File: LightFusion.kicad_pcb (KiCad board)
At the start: 2 copper layers, 52 x 52 mm, 30 parts, among them J1 303C-C4115-30-04, P1 PHR-2, U1 BMD-350-A-R, U2 TPS7A2033PDBVR, U3 TPS22918DBVR

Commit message: placement finished on PCB
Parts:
- added C_ADC_AVDD_BULK1: 100 nF, LightFusion:C_0603_1608Metric, F.Cu at (149.9, 142.6)
- added C_ADC_AVDD_BYP1: 100 nF, LightFusion:C_0603_1608Metric, F.Cu at (151.5, 142.6)
- added C_ADC_DVDD_BULK1: 1uF, LightFusion:C_0603_1608Metric, F.Cu at (156.6, 143.5)
- added C_ADC_DVDD_BYP1: 100 nF, LightFusion:C_0603_1608Metric, F.Cu at (158.8, 145.2)
- added C_ADC_PHOTO_N1: 100nF, LightFusion:C_0603_1608Metric, F.Cu at (147.3, 150.9)
- added C_ADC_PHOTO_P1: 100nF, LightFusion:C_0603_1608Metric, F.Cu at (147.3, 149.4)
- added C_ADC_REF_BULK1: 10uF, LightFusion:C_0603_1608Metric, F.Cu at (147.2, 144.5)
- added C_ADC_REF_BYP1: 100 nF, LightFusion:C_0603_1608Metric, F.Cu at (147.2, 146.2)
- added C_PD_BIAS1: 10uF, LightFusion:C_0603_1608Metric, F.Cu at (145.0, 135.6)
- added C_PD_FB1: 6.8pF, LightFusion:C_0603_1608Metric, F.Cu at (141.3, 140.5)
- added C_PD_TIA_SUPPLY1: 1 µF, LightFusion:C_0603_1608Metric, F.Cu at (143.0, 144.7)
- added D_PD1: VEMD8082, LightFusion:VEMD8082, F.Cu at (150.1, 137.3)
- added IC1: MCP3561T-E_ST, LightFusion:MCP3561T-E_ST, F.Cu at (153.1, 148.1)
- added R_ADC_CS_PU1: 10k, LightFusion:R_0603_1608Metric, F.Cu at (158.8, 147.1)
- added R_ADC_IRQ_PU1: 10k, LightFusion:R_0603_1608Metric, F.Cu at (158.8, 149.6)
- added R_ADC_PHOTO_N1: 100R, LightFusion:R_0603_1608Metric, F.Cu at (147.3, 152.5)
- added R_ADC_PHOTO_P1: 100R, LightFusion:R_0603_1608Metric, F.Cu at (147.3, 147.8)
- added R_PD_BIAS_BOT1: 1.8k, LightFusion:R_0603_1608Metric, F.Cu at (143.4, 135.6)
- added R_PD_BIAS_TOP1: 10k, LightFusion:R_0603_1608Metric, F.Cu at (141.8, 135.6)
- added R_PD_FB1: 10k, LightFusion:R_0603_1608Metric, F.Cu at (139.8, 140.5)
- added R_PD_SUPPLY1: 10R, LightFusion:R_0603_1608Metric, F.Cu at (140.2, 135.7)
- added U_PD_TIA1: OPA381AIDGKR, LightFusion:OPA381AIDGKR, F.Cu at (143.9, 140.6)
- C730_BYP1, C850_BYP1, CSLOPE_730, CSLOPE_850, C_M1, C_M2, C_PWR3, C_PWR4, C_PWR_SW_CT1, C_TEMP1: footprint LightFusion:C_0402_1005Metric -> LightFusion:C_0603_1608Metric
- J1: footprint LightFusion:303D-L186M020 -> LightFusion:303D-L186F020
- R1, R2, R_ON_PD1, R_TEMP_ALERT1: footprint LightFusion:R_0402_1005Metric -> LightFusion:R_0603_1608Metric
- moved U1 15.6 mm to (164.0, 115.1), turned to -135 degrees
- moved R2 12.8 mm to (158.5, 118.4), turned to 45 degrees
- moved C_M2 12.3 mm to (161.2, 120.9), turned to -135 degrees
- moved R1 11.9 mm to (159.8, 119.6), turned to 45 degrees
- moved J_PROG1 7.86 mm to (167.8, 124.1), turned to 180 degrees
- moved C_PWR3 7.84 mm to (147.6, 120.0)
- moved C_M1 7.22 mm to (165.6, 120.5), turned to 0 degrees
- moved U2 7.18 mm to (149.7, 122.8)
- moved C_PWR4 7.16 mm to (150.9, 120.0)
- moved C_PWR_SW_CT1 6.20 mm to (153.4, 123.3), turned to 90 degrees
- moved U3 5.66 mm to (154.6, 119.4)
- moved R_ON_PD1 3.45 mm to (155.7, 113.6)
- moved CSLOPE_850 1.38 mm to (167.6, 129.0), turned to 0 degrees
- moved U_TEMP1 1.22 mm to (150.0, 128.8)
- moved R_TEMP_ALERT1 0.72 mm to (149.1, 131.5)
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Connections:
- U1 pad 10: unconnected-(U1-P0.17-Pad10) -> ADC_MISO
- U1 pad 11: unconnected-(U1-P0.15-Pad11) -> ADC_SCK
- U1 pad 13: unconnected-(U1-P0.12-Pad13) -> ADC_CS_N
- U1 pad 42: unconnected-(U1-P0.19-Pad42) -> ADC_DRDY_N
- U1 pad 8: unconnected-(U1-P0.18-Pad8) -> ADC_MOSI

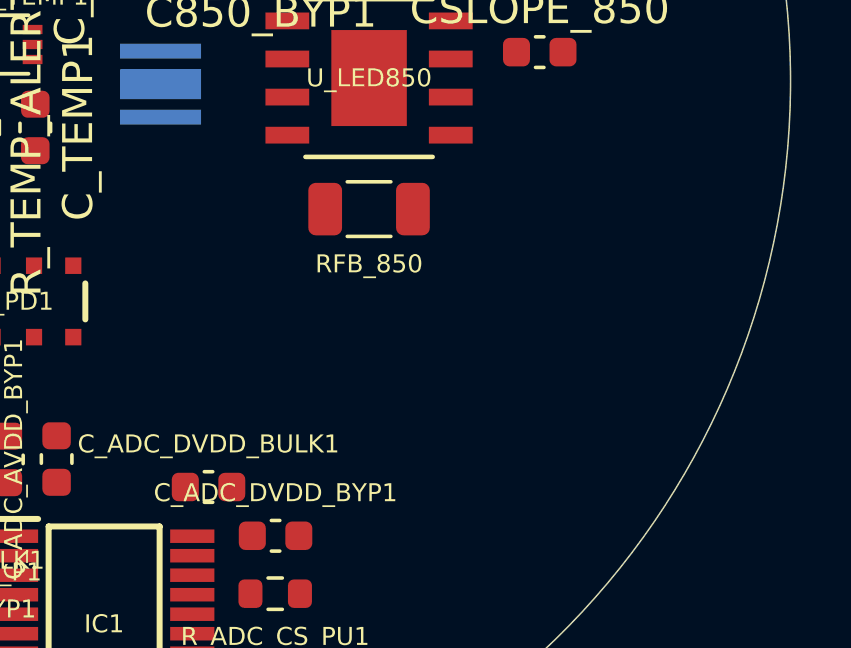
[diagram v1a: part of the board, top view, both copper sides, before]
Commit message: eeg ic was added
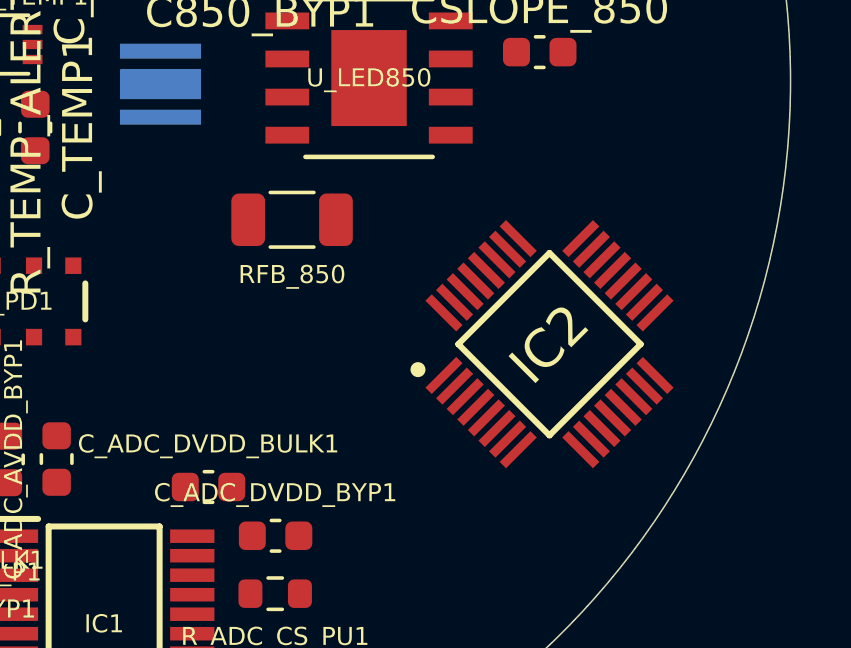
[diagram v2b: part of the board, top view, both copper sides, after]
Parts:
- added IC2: ADS1291IPBSR, LightFusion:ADS1291IPBSR, F.Cu at (168.0, 138.8)
- moved RFB_850 2.59 mm to (159.4, 134.6)

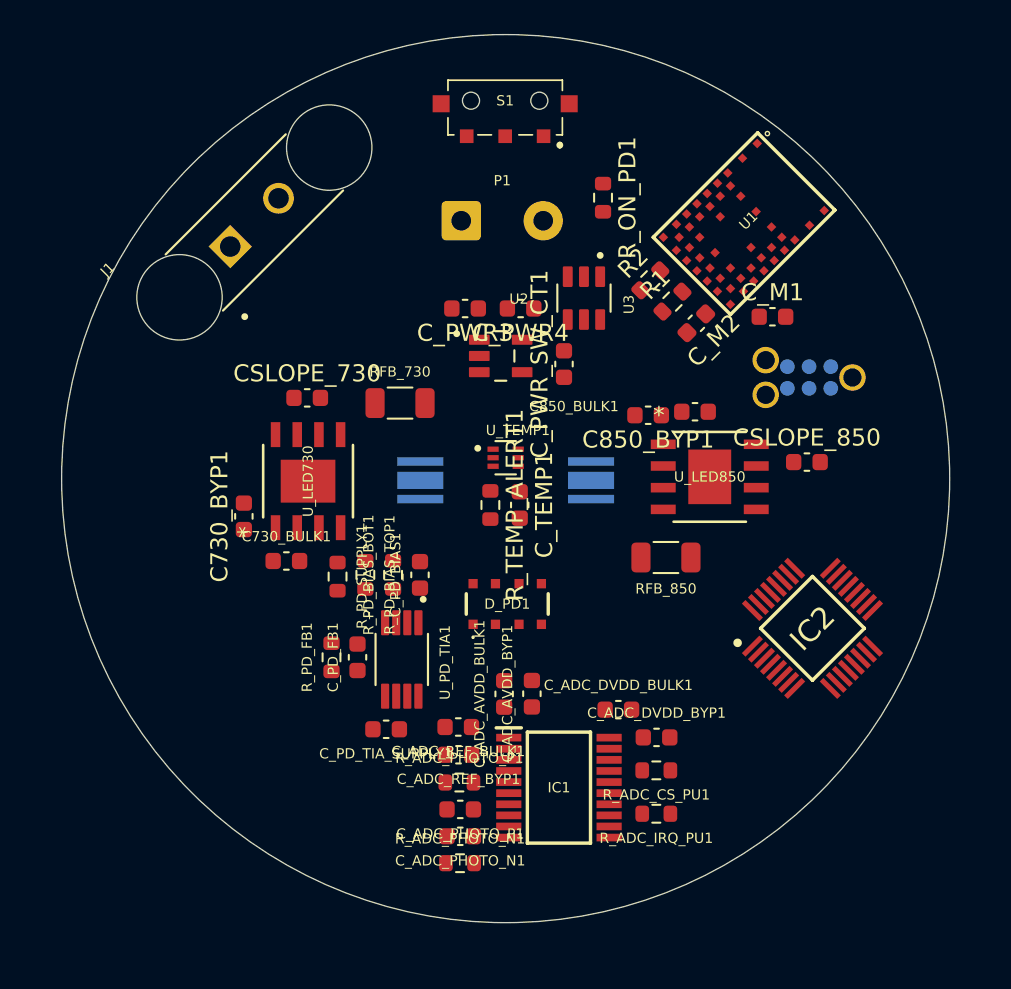
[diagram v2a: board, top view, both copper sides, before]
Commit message: eeg part refactored electrodes
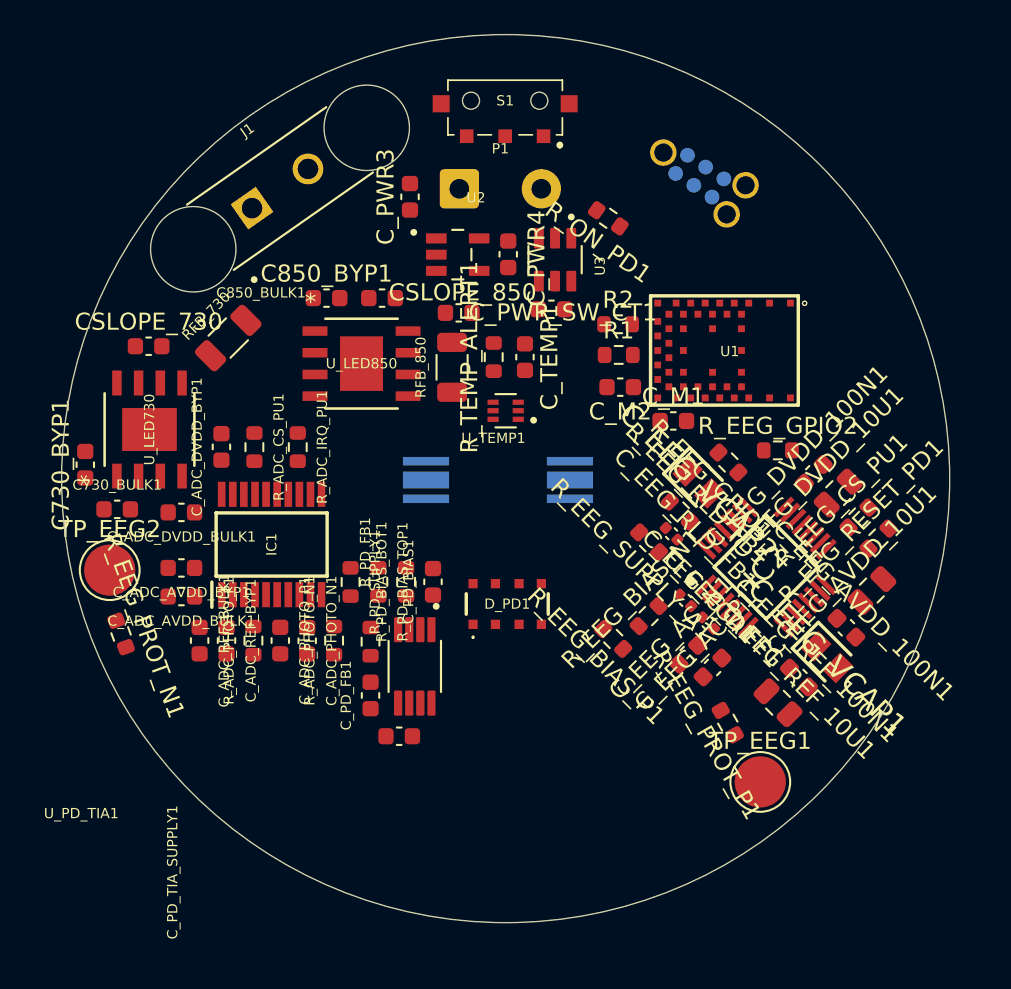
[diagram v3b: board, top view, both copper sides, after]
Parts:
- added C_EEG_AC_N1: 47 nF, LightFusion:C_0603_1608Metric, F.Cu at (160.7, 140.3)
- added C_EEG_AC_P1: 47 nF, LightFusion:C_0603_1608Metric, F.Cu at (162.1, 141.1)
- added C_EEG_AVDD_100N1: 100 nF, LightFusion:C_0603_1608Metric, F.Cu at (169.9, 138.7)
- added C_EEG_AVDD_10U1: 10 µF, LightFusion:C_0805_2012Metric, F.Cu at (171.4, 136.6)
- added C_EEG_DIFF1: 2.2 nF, LightFusion:C_0402_1005Metric, F.Cu at (161.9, 138.5)
- added C_EEG_DVDD_100N1: 100 nF, LightFusion:C_0603_1608Metric, F.Cu at (168.0, 129.7)
- added C_EEG_DVDD_10U1: 10 µF, LightFusion:C_0805_2012Metric, F.Cu at (169.5, 130.8)
- added C_EEG_PGA1: 4.7 nF, LightFusion:C_0402_1005Metric, F.Cu at (160.5, 137.1)
- added C_EEG_REF_100N1: 100 nF, LightFusion:C_0603_1608Metric, F.Cu at (167.2, 141.7)
- added C_EEG_REF_10U1: 10 µF, LightFusion:C_0805_2012Metric, F.Cu at (165.9, 143.1)
- added C_EEG_RLD_FB1: 1.5 nF, LightFusion:C_0402_1005Metric, F.Cu at (159.7, 133.2)
- added C_EEG_VCAP1: 1 µF, LightFusion:CAPPC2012X90N, F.Cu at (168.8, 140.5)
- added C_EEG_VCAP2: 1 µF, LightFusion:CAPPC2012X90N, F.Cu at (161.3, 130.2)
- added R_EEG_BIAS_N1: 22 MΩ, LightFusion:R_0603_1608Metric, F.Cu at (158.4, 138.0)
- added R_EEG_BIAS_P1: 22 MΩ, LightFusion:R_0603_1608Metric, F.Cu at (156.3, 139.4)
- added R_EEG_CS_PU1: 100 kΩ, LightFusion:R_0603_1608Metric, F.Cu at (170.7, 132.3)
- added R_EEG_GPIO1: 10 kΩ, LightFusion:R_0603_1608Metric, F.Cu at (163.0, 129.1)
- added R_EEG_GPIO2: 10 kΩ, LightFusion:R_0603_1608Metric, F.Cu at (165.9, 128.3)
- added R_EEG_PROT_N1: 51 kΩ, LightFusion:R_0603_1608Metric, F.Cu at (127.5, 139.1)
- added R_EEG_PROT_P1: 51 kΩ, LightFusion:R_0603_1608Metric, F.Cu at (163.0, 144.3)
- added R_EEG_RESET_PD1: 100 kΩ, LightFusion:R_0603_1608Metric, F.Cu at (171.8, 133.5)
- added R_EEG_RLD_FB1: 1 MΩ, LightFusion:R_0603_1608Metric, F.Cu at (160.2, 131.9)
- added R_EEG_SUPPLY_A1: 10 Ω, LightFusion:R_0603_1608Metric, F.Cu at (158.4, 133.7)
- added TP_EEG1: TestPoint, LightFusion:TestPoint_Pad_D3.0mm, F.Cu at (164.9, 147.8)
- added TP_EEG2: TestPoint, LightFusion:TestPoint_Pad_D3.0mm, F.Cu at (126.8, 135.4)
- moved C_ADC_DVDD_BYP1 30.6 mm to (133.4, 128.1), turned to 90 degrees
- moved R_ADC_CS_PU1 30.2 mm to (135.3, 128.2), turned to -90 degrees
- moved R_ADC_IRQ_PU1 30.0 mm to (137.8, 128.2), turned to -90 degrees
- moved C_ADC_DVDD_BULK1 28.1 mm to (131.0, 132.0), turned to 180 degrees
- moved CSLOPE_850 22.2 mm to (147.3, 120.3)
- moved IC1 22.0 mm to (136.3, 133.9), turned to 90 degrees
- moved C_ADC_AVDD_BYP1 21.8 mm to (131.0, 135.2), turned to 180 degrees
- moved U_LED850 21.4 mm to (141.6, 123.3)
- moved C850_BYP1 20.0 mm to (139.5, 119.4), turned to 0 degrees
- moved C_ADC_AVDD_BULK1 19.7 mm to (131.0, 136.9), turned to 180 degrees
- moved C850_BULK1 19.5 mm to (142.8, 119.4)
- moved RFB_850 16.8 mm to (146.9, 123.5), turned to 90 degrees
- moved C_ADC_REF_BULK1 16.0 mm to (132.1, 139.5), turned to -90 degrees
- moved C_ADC_REF_BYP1 15.1 mm to (133.7, 139.5), turned to -90 degrees
- moved R_ADC_PHOTO_N1 15.0 mm to (140.0, 139.5), turned to 90 degrees
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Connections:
- IC2 pad 1: unconnected-(IC2-PGA1N-Pad1) -> Net-(IC2-PGA1N)
- IC2 pad 10: unconnected-(IC2-VREFN-Pad10) -> GND
- IC2 pad 11: unconnected-(IC2-VCAP1-Pad11) -> Net-(IC2-VCAP1)
- IC2 pad 12: unconnected-(IC2-AVDD-Pad12) -> /3V3_EEG_A
- IC2 pad 13: unconnected-(IC2-AVSS-Pad13) -> GND
- IC2 pad 14: unconnected-(IC2-CLKSEL-Pad14) -> 3V3_DIG
- IC2 pad 15: unconnected-(IC2-~{PWDN}/~{RESET}-Pad15) -> /EEG_RESET_N
- IC2 pad 16: unconnected-(IC2-START-Pad16) -> GND
- IC2 pad 18: unconnected-(IC2-~{CS}-Pad18) -> /EEG_CS_N
- IC2 pad 19: unconnected-(IC2-DIN-Pad19) -> ADC_MOSI
- IC2 pad 2: unconnected-(IC2-PGA1P-Pad2) -> Net-(IC2-PGA1P)
- IC2 pad 20: unconnected-(IC2-SCLK-Pad20) -> ADC_SCK
- IC2 pad 21: unconnected-(IC2-DOUT-Pad21) -> ADC_MISO
- IC2 pad 22: unconnected-(IC2-~{DRDY}-Pad22) -> /EEG_DRDY
- IC2 pad 23: unconnected-(IC2-DVDD-Pad23) -> 3V3_DIG
- IC2 pad 24: unconnected-(IC2-DGND-Pad24) -> GND
- IC2 pad 25: unconnected-(IC2-GPIO2/RCLK2-Pad25) -> Net-(IC2-GPIO2/RCLK2)
- IC2 pad 26: unconnected-(IC2-GPIO1/RCLK1-Pad26) -> Net-(IC2-GPIO1/RCLK1)
- IC2 pad 27: unconnected-(IC2-VCAP2-Pad27) -> Net-(IC2-VCAP2)
- IC2 pad 28: unconnected-(IC2-RLDINV-Pad28) -> Net-(IC2-RLDINV)
- IC2 pad 29: unconnected-(IC2-RLDIN/RLDREF-Pad29) -> /3V3_EEG_A
- IC2 pad 3: unconnected-(IC2-IN1N-Pad3) -> Net-(IC2-IN1N)
- IC2 pad 30: unconnected-(IC2-RLDOUT-Pad30) -> /EEG_BIAS
- IC2 pad 31: unconnected-(IC2-RESP_MODP/IN3P-Pad31) -> /3V3_EEG_A
- IC2 pad 32: unconnected-(IC2-RESP_MODN/IN3N-Pad32) -> /3V3_EEG_A
- IC2 pad 4: unconnected-(IC2-IN1P-Pad4) -> Net-(IC2-IN1P)
- IC2 pad 5: unconnected-(IC2-IN2N-Pad5) -> /3V3_EEG_A
- IC2 pad 6: unconnected-(IC2-IN2P-Pad6) -> /3V3_EEG_A
- IC2 pad 9: unconnected-(IC2-VREFP-Pad9) -> Net-(IC2-VREFP)
- U1 pad 41: unconnected-(U1-P0.22-Pad41) -> /EEG_RESET_N
- U1 pad 6: unconnected-(U1-P0.20-Pad6) -> /EEG_DRDY
- U1 pad 9: unconnected-(U1-P0.16-Pad9) -> /EEG_CS_N

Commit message: added pogo electrodes
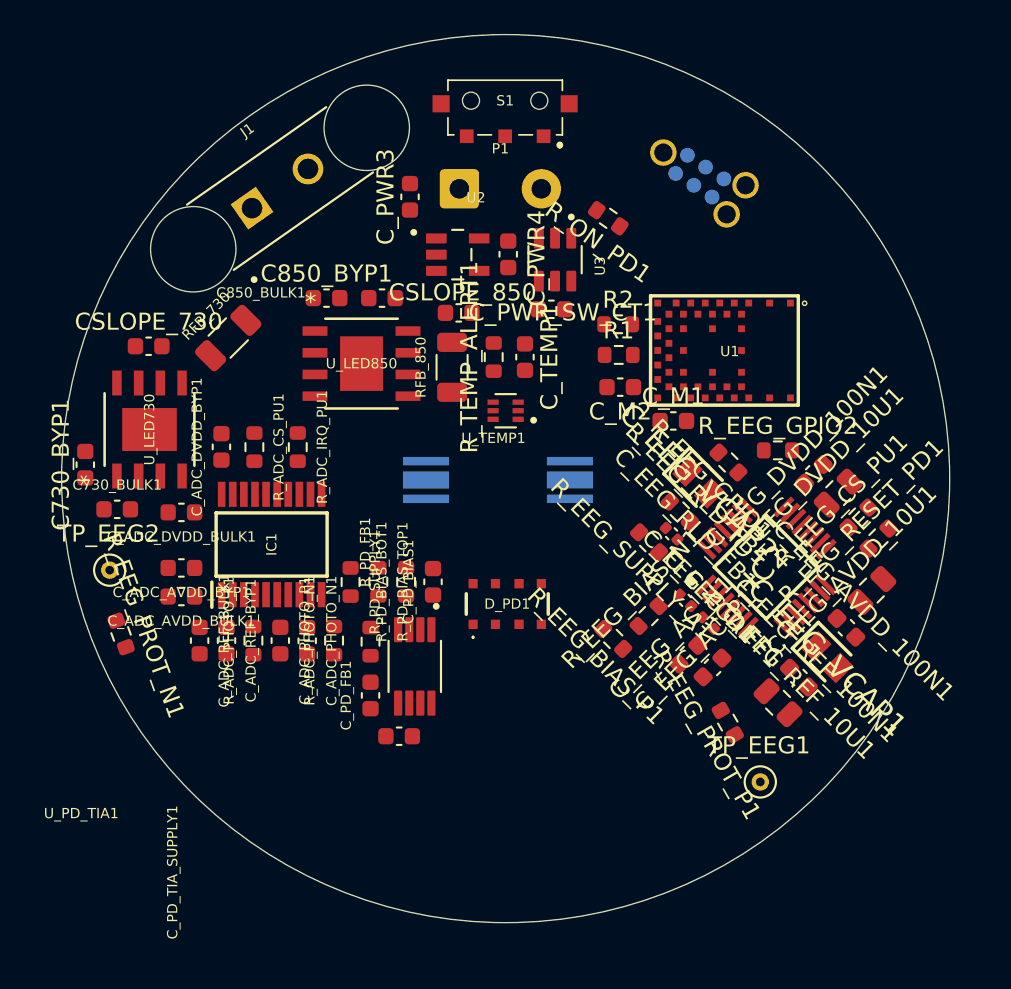
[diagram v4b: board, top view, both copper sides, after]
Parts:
- TP_EEG1, TP_EEG2: footprint LightFusion:TestPoint_Pad_D3.0mm -> LightFusion:MILL-MAX_0906-0-15-20-76-14-11-0
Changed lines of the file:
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@@
 		)
 	)
-	(footprint "LightFusion:TestPoint_Pad_D3.0mm"
+	(footprint "LightFusion:MILL-MAX_0906-0-15-20-76-14-11-0"
 		(layer "F.Cu")
 		(at 164.91 147.76)
-		(descr "SMD pad as test Point, diameter 3.0mm")
-		(tags "test point SMD pad")
 		(property "Reference" "TP_EEG1"
-			(at 0 -2.398 0)
+			(at -0.075 -2.135 0)
 			(layer "F.SilkS")
 			(effects
@@
 		)
 		(property "Value" "TestPoint"
-			(at 0 2.55 0)
+			(at 17.07 2.135 0)
 			(layer "F.Fab")
-			(hide yes)
 			(effects
 				(font
@@
 		(property "Datasheet" ""
 			(at 0 0 0)
-			(unlocked yes)
 			(layer "F.Fab")
 			(hide yes)
@@
 				(font
 					(size 1.27 1.27)
-					(thickness 0.15)
 				)
 			)
@@
 		(property "Description" "test point"
 			(at 0 0 0)
-			(unlocked yes)
 			(layer "F.Fab")
 			(hide yes)
@@
 				(font
 					(size 1.27 1.27)
-					(thickness 0.15)
 				)
 			)
@@
 			)
 		)
+		(attr through_hole)
 		(duplicate_pad_numbers_are_jumpers no)
 		(fp_circle
 			(center 0 0)
-			(end 0 1.75)
+			(end 0.9144 0)
 			(stroke
-				(width 0.12)
+				(width 0.127)
 				(type solid)
 			)
@@
 		(fp_circle
 			(center 0 0)
-			(end 2 0)
+			(end 1.1644 0)
 			(stroke
 				(width 0.05)
@@
 			(layer "F.CrtYd")
 		)
-		(fp_text user "${REFERENCE}"
-			(at 0 -2.4 0)
-			(layer "F.Fab")
-			(effects
-				(font
-					(size 1 1)
-					(thickness 0.15)
-				)
+		(fp_circle
+			(center 0 0)
+			(end 0.9144 0)
+			(stroke
+				(width 0.127)
+				(type solid)
 			)
+			(fill no)
+			(layer "F.Fab")
 		)
-		(pad "1" smd circle
+		(pad "1" thru_hole circle
 			(at 0 0)
-			(size 3 3)
-			(layers "F.Cu" "F.Mask")
+			(size 1.016 1.016)
+			(drill 0.508)
+			(layers "*.Cu" "*.Mask")
+			(remove_unused_layers no)
 			(net "Net-(R_EEG_PROT_P1-Pad1)")
 			(pinfunction "1_1")
 			(pintype "passive")
+			(solder_mask_margin 0.102)
 		)
 		(embedded_fonts no)
@@
 		)
 	)
-	(footprint "LightFusion:TestPoint_Pad_D3.0mm"
+	(footprint "LightFusion:MILL-MAX_0906-0-15-20-76-14-11-0"
 		(layer "F.Cu")
 		(at 126.815 135.36)
-		(descr "SMD pad as test Point, diameter 3.0mm")
-		(tags "test point SMD pad")
 		(property "Reference" "TP_EEG2"
-			(at 0 -2.398 0)
+			(at -0.075 -2.135 0)
 			(layer "F.SilkS")
 			(effects
@@
 		)
 		(property "Value" "TestPoint"
-			(at 0 2.55 0)
+			(at 17.07 2.135 0)
 			(layer "F.Fab")
-			(hide yes)
 			(effects
 				(font
@@
 		(property "Datasheet" ""
 			(at 0 0 0)
-			(unlocked yes)
 			(layer "F.Fab")
 			(hide yes)
@@
 				(font
 					(size 1.27 1.27)
-					(thickness 0.15)
 				)
 			)
@@
 		(property "Description" "test point"
 			(at 0 0 0)
-			(unlocked yes)
 			(layer "F.Fab")
 			(hide yes)
@@
 				(font
 					(size 1.27 1.27)
-					(thickness 0.15)
 				)
 			)
@@
 			)
 		)
+		(attr through_hole)
 		(duplicate_pad_numbers_are_jumpers no)
 		(fp_circle
 			(center 0 0)
-			(end 0 1.75)
+			(end 0.9144 0)
 			(stroke
-				(width 0.12)
+				(width 0.127)
 				(type solid)
 			)
@@
 		(fp_circle
 			(center 0 0)
-			(end 2 0)
+			(end 1.1644 0)
 			(stroke
 				(width 0.05)
@@
 			(layer "F.CrtYd")
 		)
-		(fp_text user "${REFERENCE}"
-			(at 0 -2.4 0)
-			(layer "F.Fab")
-			(effects
-				(font
-					(size 1 1)
-					(thickness 0.15)
-				)
+		(fp_circle
+			(center 0 0)
+			(end 0.9144 0)
+			(stroke
+				(width 0.127)
+				(type solid)
 			)
+			(fill no)
+			(layer "F.Fab")
 		)
-		(pad "1" smd circle
+		(pad "1" thru_hole circle
 			(at 0 0)
-			(size 3 3)
-			(layers "F.Cu" "F.Mask")
+			(size 1.016 1.016)
+			(drill 0.508)
+			(layers "*.Cu" "*.Mask")
+			(remove_unused_layers no)
 			(net "Net-(R_EEG_PROT_N1-Pad1)")
 			(pinfunction "1_1")
 			(pintype "passive")
+			(solder_mask_margin 0.102)
 		)
 		(embedded_fonts no)
